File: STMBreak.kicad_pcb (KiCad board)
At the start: 2 copper layers, 35.6 x 31.2 mm, 12 parts, among them J1 Conn_01x04_Pin, J2 USB_C_Receptacle_USB2.0_14P, U1 AMS1117-3.3, U2 AS5600, U3 STM32F103C8Tx, Y1 8M

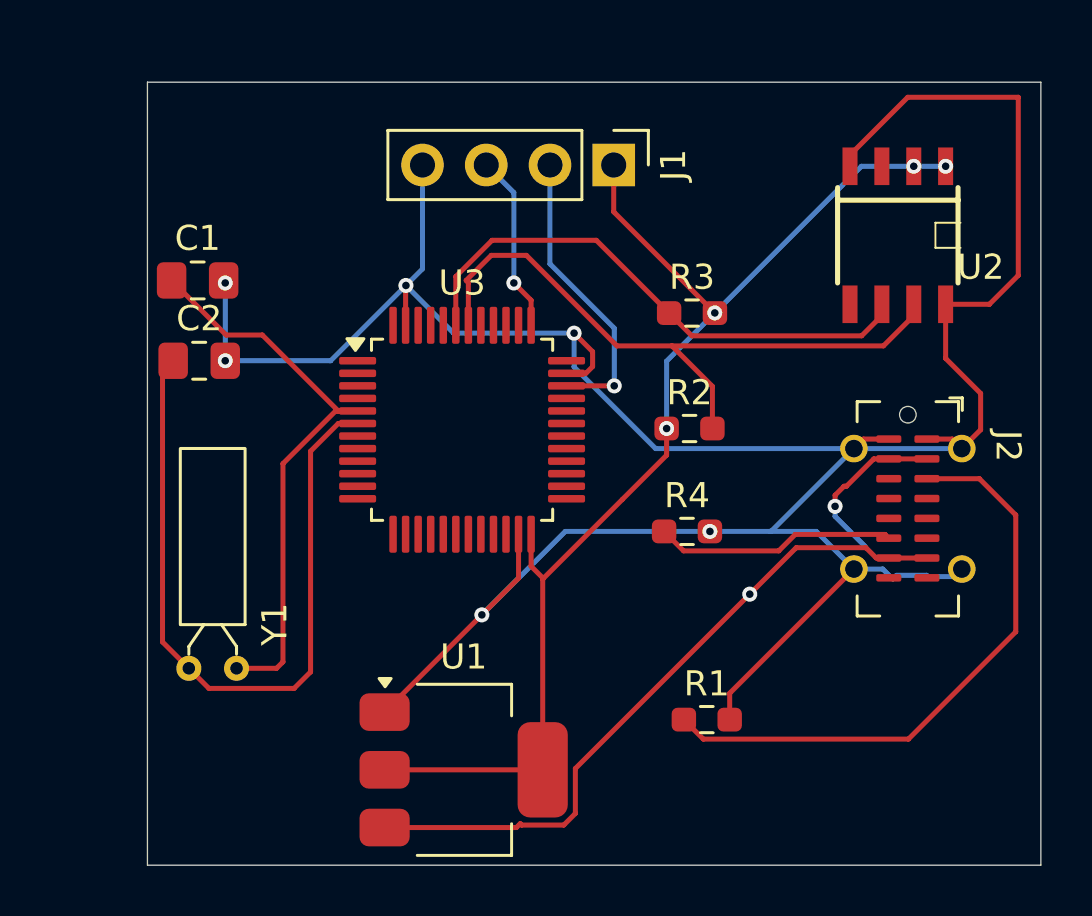
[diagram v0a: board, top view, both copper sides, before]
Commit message: Add files via upload
Capacitors, ferrite beads and other components added. Traces modified. Ground plane added.
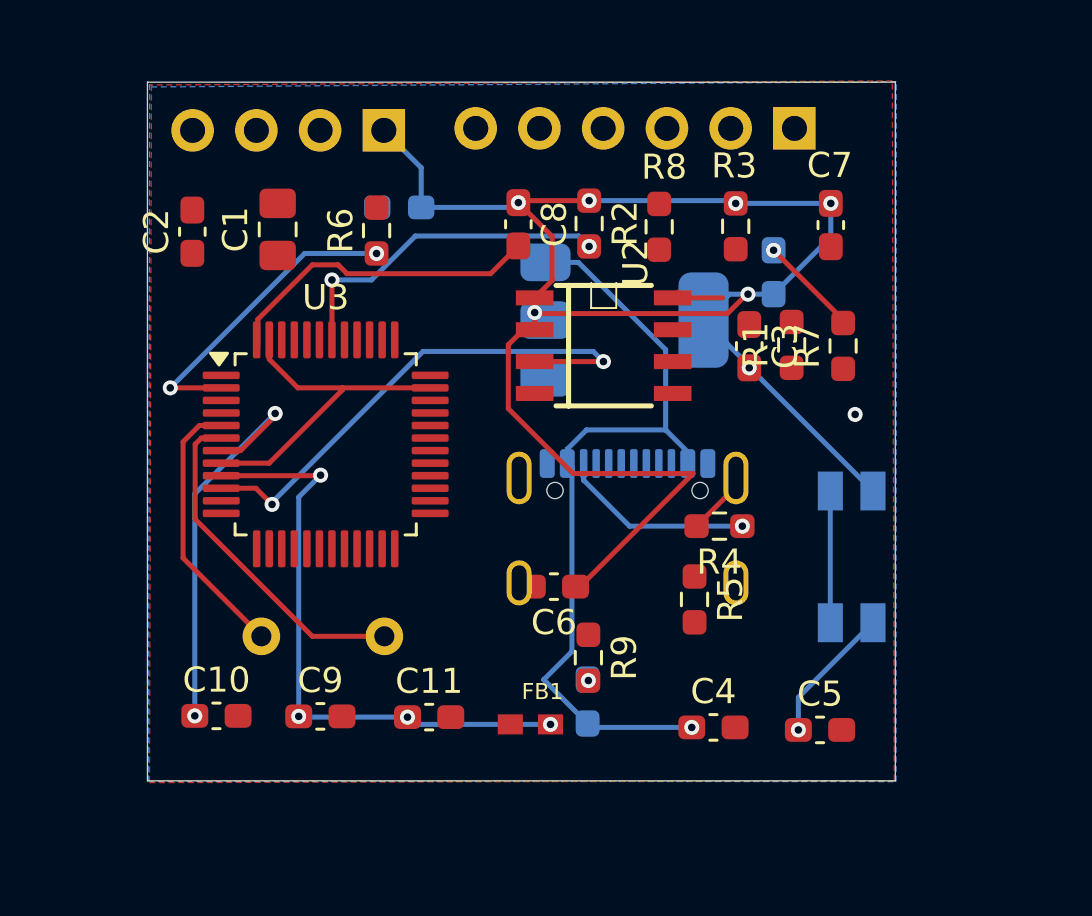
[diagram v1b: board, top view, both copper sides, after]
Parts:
- added C10: 100n, Capacitor_SMD:C_0603_1608Metric_Pad1.08x0.95mm_HandSolder, F.Cu at (163.3, 94.8)
- added C11: 10n, Capacitor_SMD:C_0603_1608Metric_Pad1.08x0.95mm_HandSolder, F.Cu at (171.8, 94.9)
- added C3: 100n, Capacitor_SMD:C_0603_1608Metric_Pad1.08x0.95mm_HandSolder, F.Cu at (184.6, 80.1)
- added C4: 10u, Capacitor_SMD:C_0603_1608Metric_Pad1.08x0.95mm_HandSolder, F.Cu at (183.2, 95.3)
- added C5: 22u, Capacitor_SMD:C_0603_1608Metric_Pad1.08x0.95mm_HandSolder, F.Cu at (187.4, 95.4)
- added C6: 100n, Capacitor_SMD:C_0603_1608Metric_Pad1.08x0.95mm_HandSolder, F.Cu at (176.8, 89.7)
- added C7: 100n, Capacitor_SMD:C_0603_1608Metric_Pad1.08x0.95mm_HandSolder, F.Cu at (187.8, 75.3)
- added C8: 100n, Capacitor_SMD:C_0603_1608Metric_Pad1.08x0.95mm_HandSolder, F.Cu at (175.4, 75.3)
- added C9: 1u, Capacitor_SMD:C_0603_1608Metric_Pad1.08x0.95mm_HandSolder, F.Cu at (167.5, 94.9)
- added D1: LED, LED_SMD:LED_0603_1608Metric_Pad1.05x0.95mm_HandSolder, B.Cu at (170.6, 74.6)
- added D2: LED, LED_SMD:LED_0603_1608Metric_Pad1.05x0.95mm_HandSolder, B.Cu at (185.6, 77.2)
- added D3: LED, LED_SMD:LED_0603_1608Metric_Pad1.05x0.95mm_HandSolder, B.Cu at (178.1, 94.3)
- added FB1: 600, FerriteBead:FB_LI0603G121R-10, F.Cu at (175.9, 95.2)
- added J3: Conn_01x06_Pin, Connector_PinSocket_2.54mm:PinSocket_1x06_P2.54mm_Vertical, B.Cu at (186.4, 71.4)
- added R5: 1k5, Resistor_SMD:R_0603_1608Metric_Pad0.98x0.95mm_HandSolder, F.Cu at (182.4, 90.2)
- added R6: 1k, Resistor_SMD:R_0603_1608Metric_Pad0.98x0.95mm_HandSolder, F.Cu at (169.7, 75.5)
- added R7: 65, Resistor_SMD:R_0603_1608Metric_Pad0.98x0.95mm_HandSolder, F.Cu at (188.3, 80.1)
- added R8: 4k7, Resistor_SMD:R_0603_1608Metric_Pad0.98x0.95mm_HandSolder, F.Cu at (181.0, 75.4)
- added R9: 150, Resistor_SMD:R_0603_1608Metric_Pad0.98x0.95mm_HandSolder, F.Cu at (178.2, 92.5)
- added SW1: SW_Push, Button_Switch_SMD:Panasonic_EVQPUJ_EVQPUA, B.Cu at (188.7, 88.5)
- C2: footprint Capacitor_SMD:C_0805_2012Metric_Pad1.18x1.45mm_HandSolder -> Capacitor_SMD:C_0603_1608Metric_Pad1.08x0.95mm_HandSolder
- J1, U1: moved to B.Cu
- J2: footprint Connector_USB:USB_C_Receptacle_G-Switch_GT-USB-7051x -> Connector_USB:USB_C_Receptacle_GCT_USB4105-xx-A_16P_TopMnt_Horizontal; moved to B.Cu
- R1, R4: value 4.7k -> 5k1
- R2, R3: value 4.7k -> 4k7
- Y1: footprint Crystal:Crystal_C26-LF_D2.1mm_L6.5mm_Horizontal -> Crystal:Crystal_HC49-U_Horizontal; moved to B.Cu
- moved U1 19.0 mm to (179.6, 79.1)
- moved R1 15.3 mm to (186.3, 80.1), turned to 90 degrees
- moved U2 12.5 mm to (178.8, 80.1), turned to -90 degrees
- moved J2 11.3 mm to (179.7, 88.5), turned to 180 degrees
- moved J1 9.26 mm to (170.0, 71.5), turned to 90 degrees
- moved R2 9.09 mm to (178.2, 75.2), turned to -90 degrees
- moved U3 5.47 mm to (167.7, 84.0)
- moved C2 5.15 mm to (162.4, 75.6), turned to 90 degrees
- moved R3 3.87 mm to (184.0, 75.3), turned to 90 degrees
- moved C1 3.78 mm to (165.8, 75.5), turned to 90 degrees
- moved Y1 1.61 mm to (165.1, 91.7), turned to 0 degrees
- moved R4 1.31 mm to (183.4, 87.3), turned to 180 degrees
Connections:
- J2 pad A6: unconnected-(J2-D+-PadA6) -> D+
- J2 pad A7: unconnected-(J2-D--PadA7) -> D-
- J2 pad B6: unconnected-(J2-D+-PadB6) -> D+
- J2 pad B7: unconnected-(J2-D--PadB7) -> D-
- U2 pad 3: unconnected-(U2-OUT-Pad3) -> OUT
- U3 pad 10: unconnected-(U3-PA0-Pad10) -> OUT
- U3 pad 12: unconnected-(U3-PA2-Pad12) -> U2TX
- U3 pad 13: unconnected-(U3-PA3-Pad13) -> U2RX
- U3 pad 2: unconnected-(U3-PC13-Pad2) -> CLED
- U3 pad 21: unconnected-(U3-PB10-Pad21) -> I2CSCL
- U3 pad 22: unconnected-(U3-PB11-Pad22) -> I2CSDA
- U3 pad 24: 3.3V -> Net-(C6-Pad2)
- U3 pad 30: unconnected-(U3-PA9-Pad30) -> UTX
- U3 pad 31: unconnected-(U3-PA10-Pad31) -> URX
- U3 pad 32: unconnected-(U3-PA11-Pad32) -> D-
- U3 pad 33: unconnected-(U3-PA12-Pad33) -> D+
- U3 pad 36: unconnected-(U3-VDD-Pad36) -> Net-(C7-Pad2)
- U3 pad 44: unconnected-(U3-BOOT0-Pad44) -> BOOT0
- U3 pad 48: unconnected-(U3-VDD-Pad48) -> Net-(C8-Pad2)
- U3 pad 7: unconnected-(U3-NRST-Pad7) -> Net-(U3-NRST)
- U3 pad 8: unconnected-(U3-VSSA-Pad8) -> GND
- U3 pad 9: unconnected-(U3-VDDA-Pad9) -> VDDA
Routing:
- net GND: track 118.5 -> 19.7 mm, vias 6 -> 1
- net 3.3V: track 48.5 -> 76.6 mm, vias 4 -> 9
- net Net-(J2-CC1): track 24.1 -> 0.00 mm
- net VDDA: track 0.00 -> 24.1 mm, vias 0 -> 4
- net SDA: track 21.9 -> 0.00 mm
- net OUT: track 0.00 -> 21.1 mm, vias 0 -> 2
- net Net-(U3-NRST): track 0.00 -> 16.2 mm, vias 0 -> 2
- net OSCOUT: track 29.4 -> 13.6 mm
- net Net-(C8-Pad2): track 0.00 -> 13.0 mm
- net SCL: track 26.5 -> 13.7 mm, vias 0 -> 2
- net CLED: track 0.00 -> 12.6 mm, vias 0 -> 2
- net OSCIN: track 23.3 -> 10.8 mm
- net SWDIO: track 11.8 -> 0.00 mm, vias 2 -> 0
- net SWCLK: track 7.13 -> 0.00 mm, vias 2 -> 0
- net BOOT0: track 0.00 -> 5.25 mm
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- added copper zone on B.Cu, net GND
- added copper zone on F.Cu, net GND
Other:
- board size 35.6 x 31.2 mm -> 29.8 x 27.8 mm

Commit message: Added D+ and D- traces with tuning.
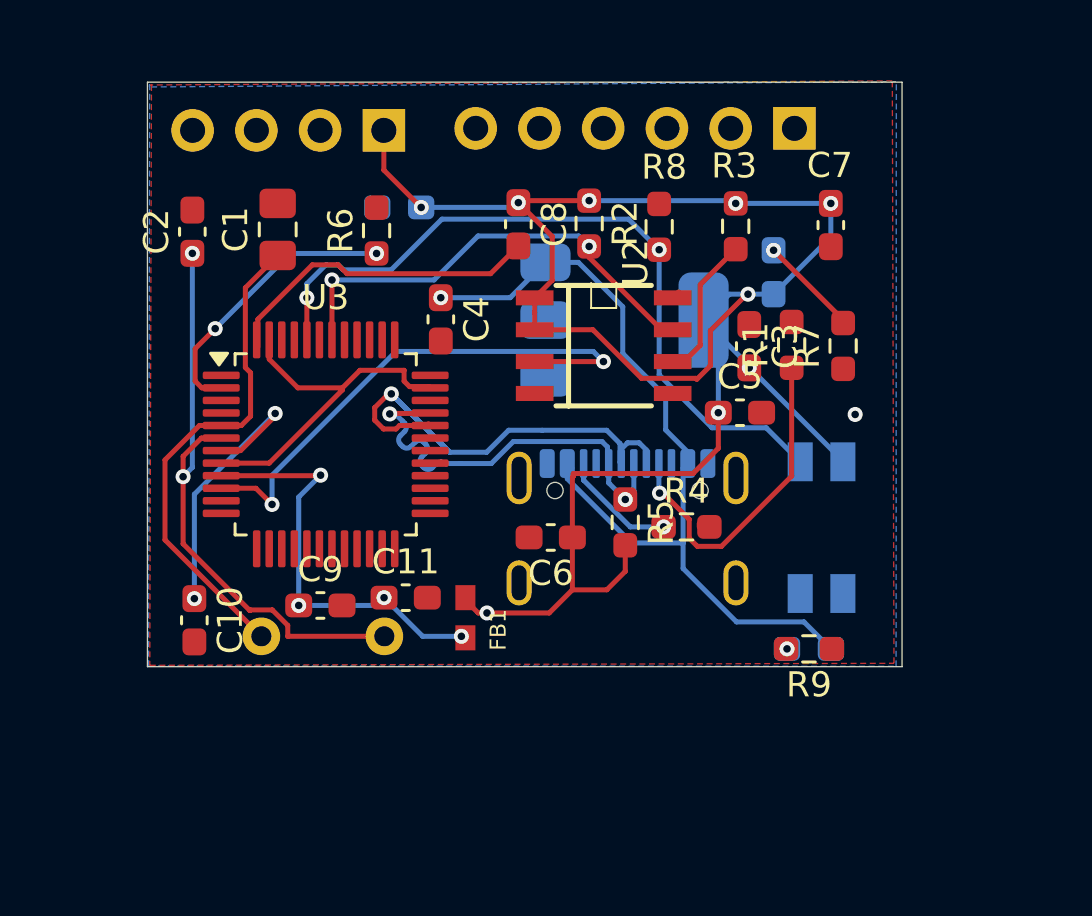
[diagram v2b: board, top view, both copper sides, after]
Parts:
- moved C4 19.6 mm to (172.3, 79.0), turned to -90 degrees
- moved C5 13.0 mm to (184.2, 82.8)
- moved D3 9.07 mm to (187.0, 92.2), turned to 0 degrees
- moved R9 8.80 mm to (187.0, 92.2), turned to 180 degrees
- moved FB1 4.98 mm to (173.3, 90.9), turned to -90 degrees
- moved C11 4.85 mm to (170.9, 90.1)
- moved C9 4.42 mm to (167.5, 90.5)
- moved R5 4.13 mm to (179.6, 87.1)
- moved C10 3.91 mm to (162.5, 91.0), turned to -90 degrees
- moved C6 1.96 mm to (176.7, 87.7)
- moved SW1 1.67 mm to (187.5, 87.3)
- moved R4 1.31 mm to (182.1, 87.3), turned to 0 degrees
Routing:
- net BOOT0: track 5.25 -> 30.1 mm, vias 0 -> 2
- net D-: track 0.00 -> 21.2 mm, vias 0 -> 1
- net D+: track 0.00 -> 17.6 mm, vias 0 -> 2
- net Net-(J2-CC1): track 0.00 -> 13.3 mm, vias 0 -> 1
- net OSCOUT: track 13.6 -> 24.2 mm, vias 0 -> 2
- net OSCIN: track 10.8 -> 19.8 mm
- net VDDA: track 24.1 -> 17.0 mm
- net SDA: track 0.00 -> 5.78 mm
- net SCL: track 13.7 -> 18.6 mm
- net Net-(U3-NRST): track 16.2 -> 11.5 mm
- net GND: track 19.7 -> 16.4 mm
- net Net-(J2-CC2): track 7.75 -> 4.62 mm
- net 5V: track 31.8 -> 33.9 mm
- net 3.3V: track 76.6 -> 78.6 mm
- net CLED: track 12.6 -> 11.2 mm
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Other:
- board size 29.8 x 27.8 mm -> 30.1 x 23.3 mm

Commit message: Add files via upload
Centered AS5600.
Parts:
- Y1: footprint Crystal:Crystal_HC49-U_Horizontal -> Crystal:Crystal_SMD_HC49-SD_HandSoldering
- moved C7 14.4 mm to (173.4, 75.5)
- moved Y1 8.14 mm to (164.2, 83.6), turned to 90 degrees
- moved R3 7.29 mm to (180.1, 81.5)
- moved U2 4.12 mm to (175.0, 81.8)
- moved U3 2.14 mm to (166.1, 82.6)
- moved C4 1.50 mm to (173.4, 78.1), turned to 180 degrees
- moved C1 0.34 mm to (166.0, 75.2)
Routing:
- net U2RX: track 0.00 -> 32.6 mm
- net U2TX: track 0.00 -> 30.3 mm
- net UTX: track 0.00 -> 23.3 mm, vias 0 -> 2
- net Net-(C8-Pad2): track 13.0 -> 33.2 mm
- net URX: track 0.00 -> 19.5 mm, vias 0 -> 4
- net 3.3V: track 78.6 -> 59.6 mm
- net SDA: track 5.78 -> 20.6 mm, vias 0 -> 3
- net SWDIO: track 0.00 -> 13.6 mm, vias 0 -> 1
- net D-: track 21.2 -> 10.6 mm, vias 1 -> 0
- net OUT: track 21.7 -> 11.4 mm, vias 2 -> 0
- net OSCOUT: track 24.2 -> 14.6 mm
- net SWCLK: track 0.00 -> 9.17 mm, vias 0 -> 2
- net Net-(C6-Pad2): track 0.00 -> 7.35 mm
- net D+: track 17.6 -> 10.9 mm, vias 2 -> 1
- net Net-(C7-Pad2): track 0.00 -> 5.79 mm
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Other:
- board size 30.1 x 23.3 mm -> 31.2 x 24.6 mm

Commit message: Add files via upload
Modified design approach.
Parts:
- added REF**: MountingHole_2.1mm, MountingHole:MountingHole_2.1mm, F.Cu at (189.0, 72.4)
- added REF**: MountingHole_2.1mm, MountingHole:MountingHole_2.1mm, F.Cu at (161.7, 90.9)
- C10, C2, FB1, R6: moved to B.Cu
- SW1: footprint Button_Switch_SMD:Panasonic_EVQPUJ_EVQPUA -> TS09:SW_TS09-63-25-R-260-SMT-TR
- Y1: footprint Crystal:Crystal_SMD_HC49-SD_HandSoldering -> Crystal:Crystal_SMD_Abracon_ABM3-2Pin_5.0x3.2mm_HandSoldering
- moved R8 15.8 mm to (165.2, 75.1)
- moved C11 14.6 mm to (159.6, 81.0), turned to 90 degrees
- moved C8 14.1 mm to (161.4, 77.1)
- moved D3 13.9 mm to (173.6, 88.6), turned to 90 degrees
- moved R9 13.5 mm to (173.6, 90.4), turned to 90 degrees
- moved C3 11.5 mm to (173.3, 78.1), turned to 180 degrees
- moved R7 11.2 mm to (178.7, 74.5), turned to 180 degrees
- moved C2 10.8 mm to (168.8, 84.3), turned to 0 degrees
- moved C9 10.0 mm to (159.5, 84.4), turned to -90 degrees
- moved FB1 9.38 mm to (165.2, 86.2), turned to 180 degrees
- moved SW1 9.32 mm to (184.1, 78.7)
- moved D2 9.11 mm to (176.8, 74.5), turned to 180 degrees
- moved R1 9.09 mm to (182.2, 88.2), turned to -90 degrees
- moved D1 7.09 mm to (163.6, 75.1), turned to 90 degrees
- moved R6 6.98 mm to (163.6, 78.9)
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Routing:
- net I2CSCL: track 0.00 -> 39.3 mm, vias 0 -> 1
- net I2CSDA: track 0.00 -> 36.6 mm, vias 0 -> 1
- net Net-(C8-Pad2): track 33.2 -> 1.88 mm
- net GND: track 18.1 -> 3.42 mm, vias 3 -> 0
- net D+: track 10.9 -> 25.0 mm, vias 1 -> 2
- net OUT: track 11.4 -> 0.00 mm
- net VDDA: track 19.4 -> 8.62 mm, vias 4 -> 1
- net Net-(J2-CC1): track 13.3 -> 2.71 mm
- net CLED: track 12.3 -> 1.80 mm, vias 0 -> 1
- net OSCIN: track 21.2 -> 12.4 mm, vias 2 -> 1
- net D-: track 10.6 -> 19.3 mm, vias 0 -> 3
- net U2RX: track 32.6 -> 25.6 mm, vias 0 -> 1
- net Net-(U3-NRST): track 10.1 -> 3.85 mm, vias 2 -> 1
- net UTX: track 23.3 -> 17.3 mm, vias 2 -> 0
- net URX: track 19.5 -> 13.6 mm, vias 4 -> 0
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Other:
- board size 31.2 x 24.6 mm -> 33 x 24.3 mm

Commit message: Add files via upload
Updated trace design.
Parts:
- moved FB1 1.42 mm to (165.4, 87.7)
- moved C9 0.61 mm to (159.8, 84.9)
- moved C11 0.61 mm to (159.8, 81.5)
- moved C10 0.39 mm to (165.3, 85.0)
- moved C1 0.28 mm to (168.2, 74.5)
- moved R8 0.16 mm to (165.3, 75.2)
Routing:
- net GND: track 3.42 -> 81.6 mm, vias 0 -> 27
- net OUT: track 0.00 -> 25.0 mm, vias 0 -> 2
- net 3.3V: track 55.1 -> 68.6 mm, vias 7 -> 9
- net SWDIO: track 12.3 -> 14.5 mm
- net SCL: track 19.8 -> 21.7 mm
- net OSCIN: track 12.4 -> 13.8 mm
- net SDA: track 19.6 -> 21.0 mm
- net U2TX: track 30.1 -> 31.0 mm, vias 1 -> 4
- net VDDA: track 8.62 -> 9.47 mm
- net 5V: track 28.1 -> 28.8 mm

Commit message: Add files via upload
Modified PCB design.
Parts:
- C1, C2: value 22p -> 30p
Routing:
- net GND: track 81.6 -> 77.4 mm, vias 27 -> 20
- net 5V: track 28.8 -> 28.0 mm
- net 3.3V: track 68.6 -> 67.9 mm
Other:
- board size 33 x 24.3 mm -> 32.9 x 23.8 mm

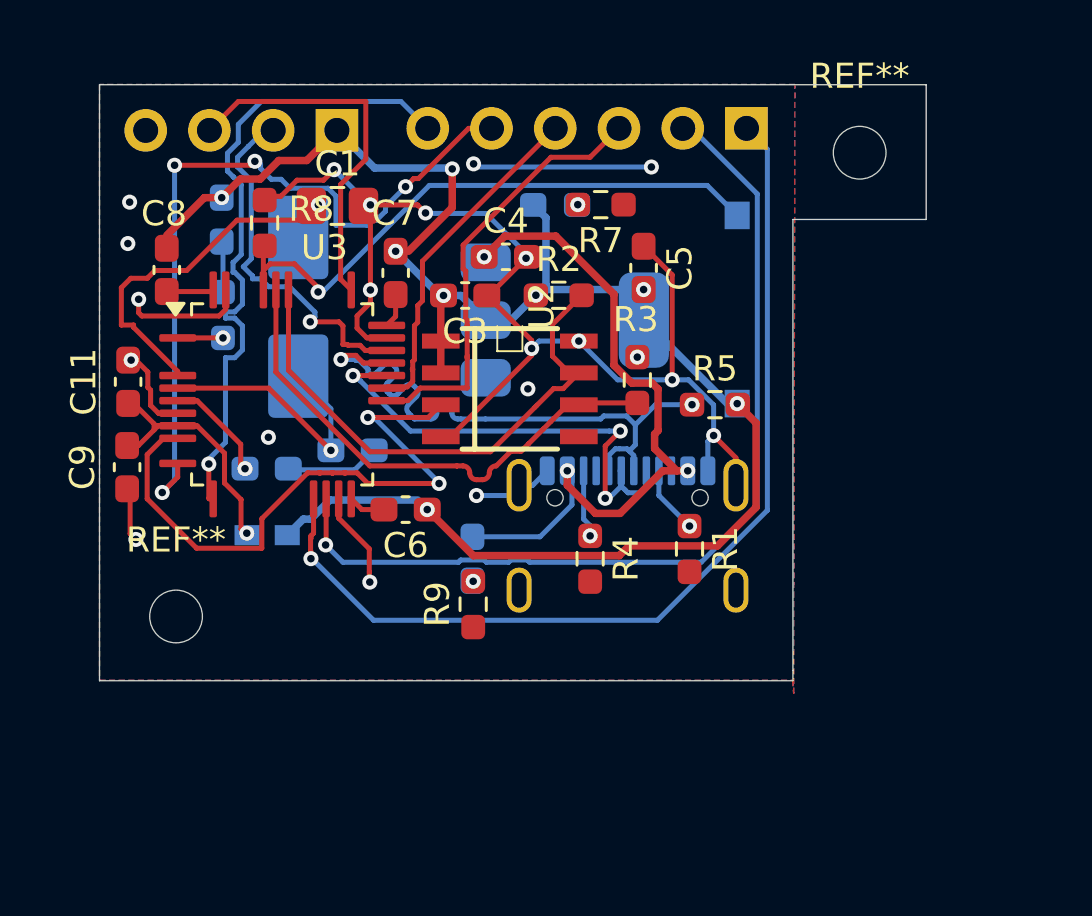
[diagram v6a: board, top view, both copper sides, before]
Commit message: Add files via upload
Mounting holes added.
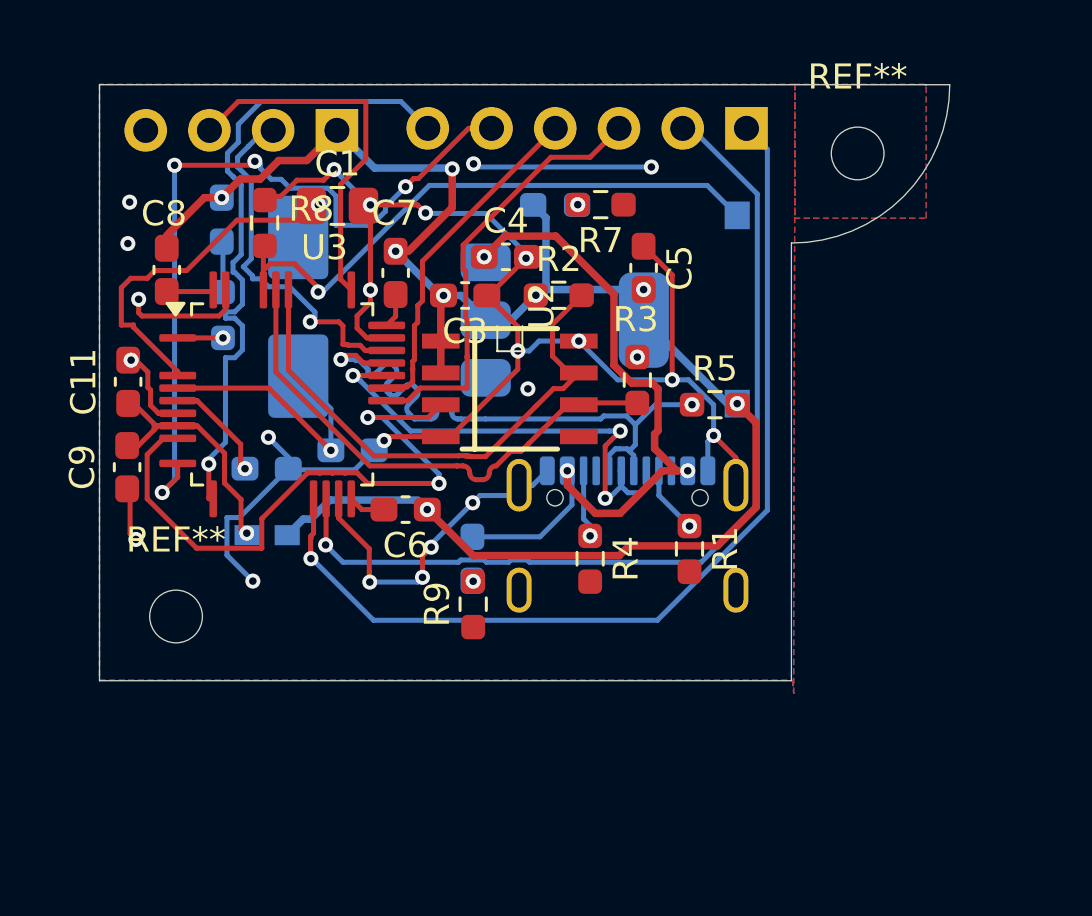
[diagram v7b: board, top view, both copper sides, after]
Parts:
- moved REF** 0.09 mm to (188.9, 72.4)
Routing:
- net GND: track 77.4 -> 94.4 mm, vias 20 -> 24
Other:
- board size 32.9 x 23.8 mm -> 33.9 x 23.8 mm

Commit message: Add files via upload
Check.
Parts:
- moved REF** 0.58 mm to (161.2, 90.9)
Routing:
- net U2RX: track 26.0 -> 24.4 mm
- net SWDIO: track 14.7 -> 13.7 mm
- net UTX: track 17.3 -> 17.9 mm
